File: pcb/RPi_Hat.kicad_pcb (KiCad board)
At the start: 2 copper layers, 65 x 56.5 mm, 31 parts, among them J1 RPi_GPIO, P1 Flow Meter, P2 Extra, P3 1 Wire, P4 Display, P5 Laser Controller, Q1 BSS138, Q2 PN2222A, Q3 BSS138, Q4 BSS138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

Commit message: Schematic updates
Don't use a relay, use a level shifter so the pin can be used as either
an input or an output.
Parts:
- removed D1: DIODE, Diodes_SMD:SMA_Handsoldering
- removed RL1: G5Q-14, Relays:Relay_SPDS_OMRON-G5Q
- added R3: 10k, Resistors_SMD:R_1206_HandSoldering, F.Cu at (102.9, 95.2)
- P2: footprint Terminal_Blocks:TerminalBlock_Pheonix_MPT-2.54mm_5pol -> Terminal_Blocks:TerminalBlock_Pheonix_MPT-2.54mm_4pol
- Q2: value PN2222A -> BSS138
- R4: value 1k -> 10k
- moved Q2 1.27 mm to (96.5, 95.2), turned to 90 degrees
- moved Q5 1.27 mm to (134.6, 82.5)
- moved R4 1.27 mm to (96.5, 91.4), turned to 180 degrees
- moved R7 1.27 mm to (130.8, 91.4)
- moved R9 1.27 mm to (130.8, 82.5)
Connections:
- net Net-(P1-Pad2) renamed FLOW_INPUT
- P2 pad 3: LP2 -> EP1
- P2 pad 4: EP1 -> +5V
- Q2 pad 1: GND -> +3V3
- Q2 pad 2: Net-(Q2-Pad2) -> LIGHTS
- Q2 pad 3: Net-(D1-Pad2) -> LP1
- R4 pad 1: Net-(Q2-Pad2) -> +5V
- R4 pad 2: LIGHTS -> LP1
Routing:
- net LP2: track 54.5 -> 0.00 mm
- net LP1: track 39.2 -> 8.57 mm
- net +3V3: track 130.4 -> 148.7 mm
- net +5V: track 142.7 -> 127.9 mm, vias 7 -> 5
- net LIGHTS: track 48.5 -> 58.8 mm
- net Net-(D1-Pad2): track 9.47 -> 0.00 mm
- net GND: track 223.0 -> 215.5 mm
- net Net-(Q2-Pad2): track 6.43 -> 0.00 mm
- net LC_AIR: track 55.4 -> 57.1 mm, vias 2 -> 0
- net LC4: track 27.0 -> 25.7 mm
- net EP1: track 13.6 -> 14.7 mm
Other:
- board text added: "Display"
- board text added: "Extra"
- board text added: "Laser"

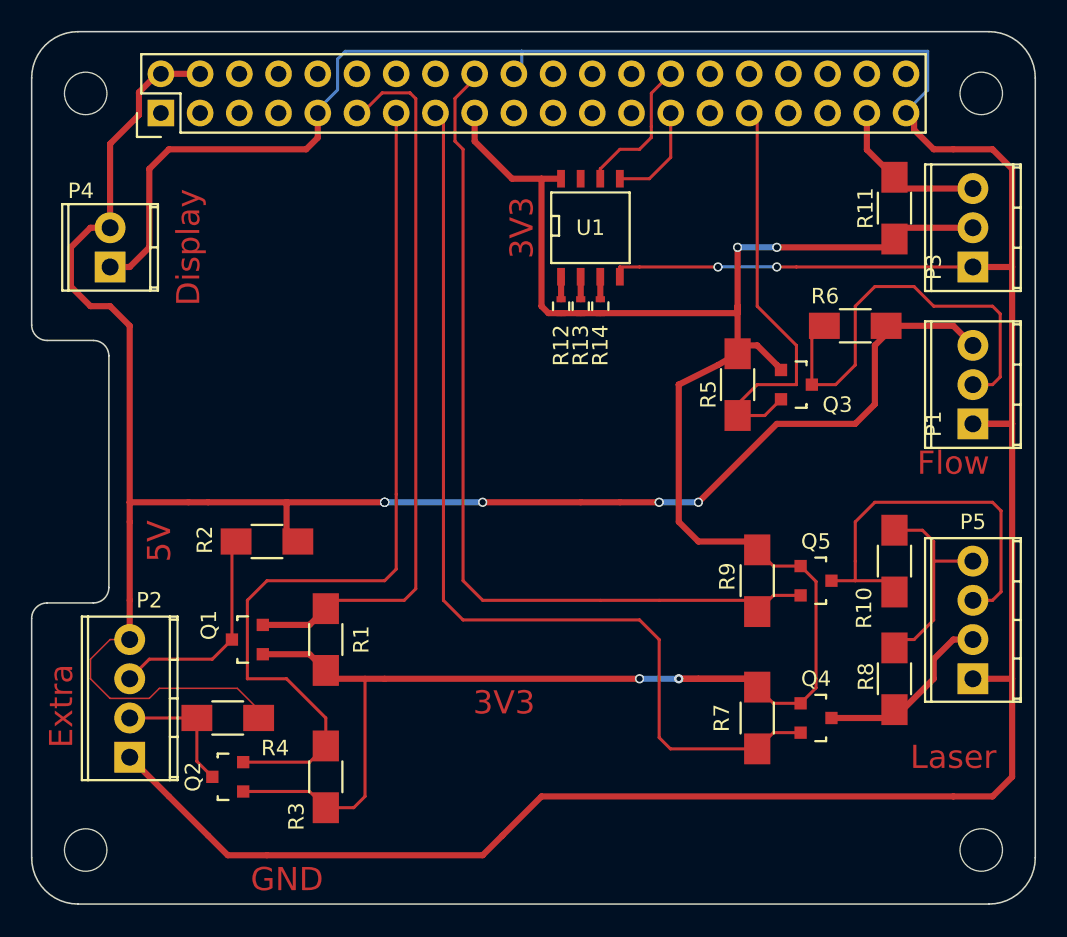
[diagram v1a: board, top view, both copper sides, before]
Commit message: Add outputs
for the chiller, exhaust, air
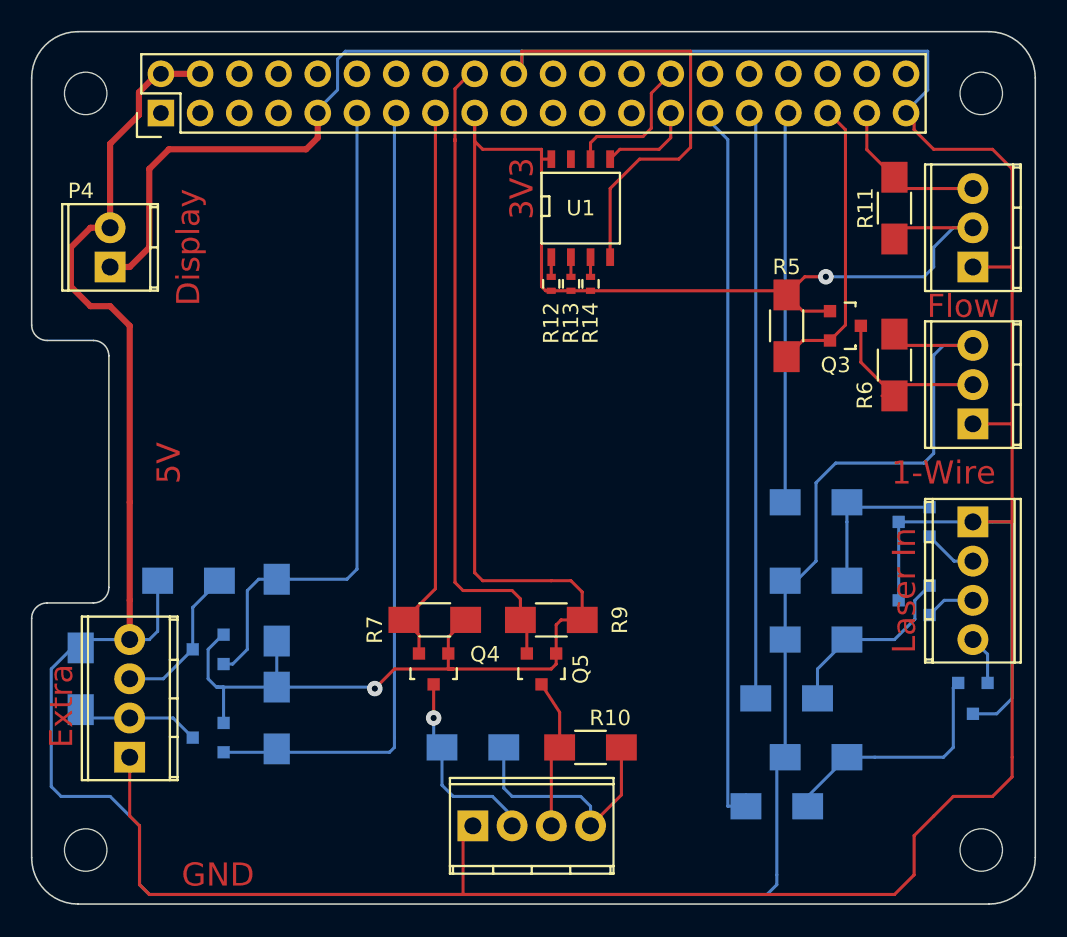
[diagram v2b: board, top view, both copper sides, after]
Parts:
- added P6: Laser Controller, Terminal_Blocks:TerminalBlock_Pheonix_MPT-2.54mm_4pol, F.Cu at (144.8, 78.7)
- added Q6: PZT2222A, TO_SOT_Packages_SMD:SOT-23, B.Cu at (144.8, 90.2)
- added Q7: PZT2222A, TO_SOT_Packages_SMD:SOT-23, B.Cu at (141.0, 83.8)
- added Q8: PZT2222A, TO_SOT_Packages_SMD:SOT-23, B.Cu at (141.0, 78.7)
- added R15: 4K7, Resistors_SMD:R_1206_HandSoldering, B.Cu at (132.1, 97.2)
- added R16: 4K7, Resistors_SMD:R_1206_HandSoldering, B.Cu at (132.7, 90.2)
- added R17: 4K7, Resistors_SMD:R_1206_HandSoldering, B.Cu at (134.6, 77.5)
- added R18: 4K7, Resistors_SMD:R_1206_HandSoldering, B.Cu at (134.6, 94.0)
- added R19: 4K7, Resistors_SMD:R_1206_HandSoldering, B.Cu at (134.6, 86.4)
- added R20: 4K7, Resistors_SMD:R_1206_HandSoldering, B.Cu at (134.6, 82.5)
- Q1, Q2, R1, R2, R3, R4, R8: moved to B.Cu
- moved P5 33.8 mm to (112.4, 98.4), turned to 0 degrees
- moved R8 27.7 mm to (112.4, 93.3), turned to 180 degrees
- moved Q4 25.0 mm to (109.9, 88.3), turned to 180 degrees
- moved R10 23.1 mm to (120.0, 93.3), turned to 0 degrees
- moved R7 21.8 mm to (109.9, 85.1), turned to 0 degrees
- moved Q5 18.7 mm to (116.8, 88.3), turned to 180 degrees
- moved R9 13.6 mm to (117.5, 85.1), turned to 0 degrees
- moved R4 9.86 mm to (87.0, 88.9), turned to 270 degrees
- moved R2 5.68 mm to (94.0, 82.5), turned to 0 degrees
- moved R3 4.96 mm to (99.7, 91.4), turned to 90 degrees
- moved Q3 4.96 mm to (136.5, 66.0)
- moved R5 4.96 mm to (132.7, 66.0)
- moved R1 3.70 mm to (99.7, 84.5)
- moved R6 3.59 mm to (139.7, 68.6), turned to 270 degrees
- moved Q2 2.84 mm to (95.2, 92.7), turned to 270 degrees
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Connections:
- J1 pad 29: (no net) -> OUT_EXHAUST
- J1 pad 31: FLOW_METER -> OUT_CHILLER
- J1 pad 33: (no net) -> OUT_AIR
- J1 pad 35: (no net) -> FLOW_METER
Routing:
- net OUT_EXHAUST: track 0.00 -> 47.3 mm
- net GND: track 215.5 -> 258.9 mm, vias 2 -> 0
- net +5V: track 127.9 -> 170.2 mm, vias 5 -> 0
- net OUT_CHILLER: track 0.00 -> 38.1 mm
- net LC_WORKING: track 63.6 -> 36.3 mm
- net OUT_AIR: track 0.00 -> 25.3 mm
- net Net-(Q6-Pad1): track 0.00 -> 16.1 mm
- net FLOW_INPUT: track 28.0 -> 12.3 mm
- net LC4: track 25.7 -> 11.0 mm
- net LC_AIR: track 57.1 -> 43.3 mm
- net Net-(Q7-Pad1): track 0.00 -> 12.2 mm
- net +3V3: track 148.7 -> 137.3 mm, vias 4 -> 2
- net Net-(Q8-Pad1): track 0.00 -> 10.6 mm
- net FLOW_METER: track 27.0 -> 18.9 mm
- net LIGHTS: track 58.8 -> 52.3 mm
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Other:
- net class Default: via_dia 0.6 -> 1
- board text added: "1-Wire"
- board text added: "Laser In"
- board text removed: "Laser"

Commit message: Add passives for the EEPROM
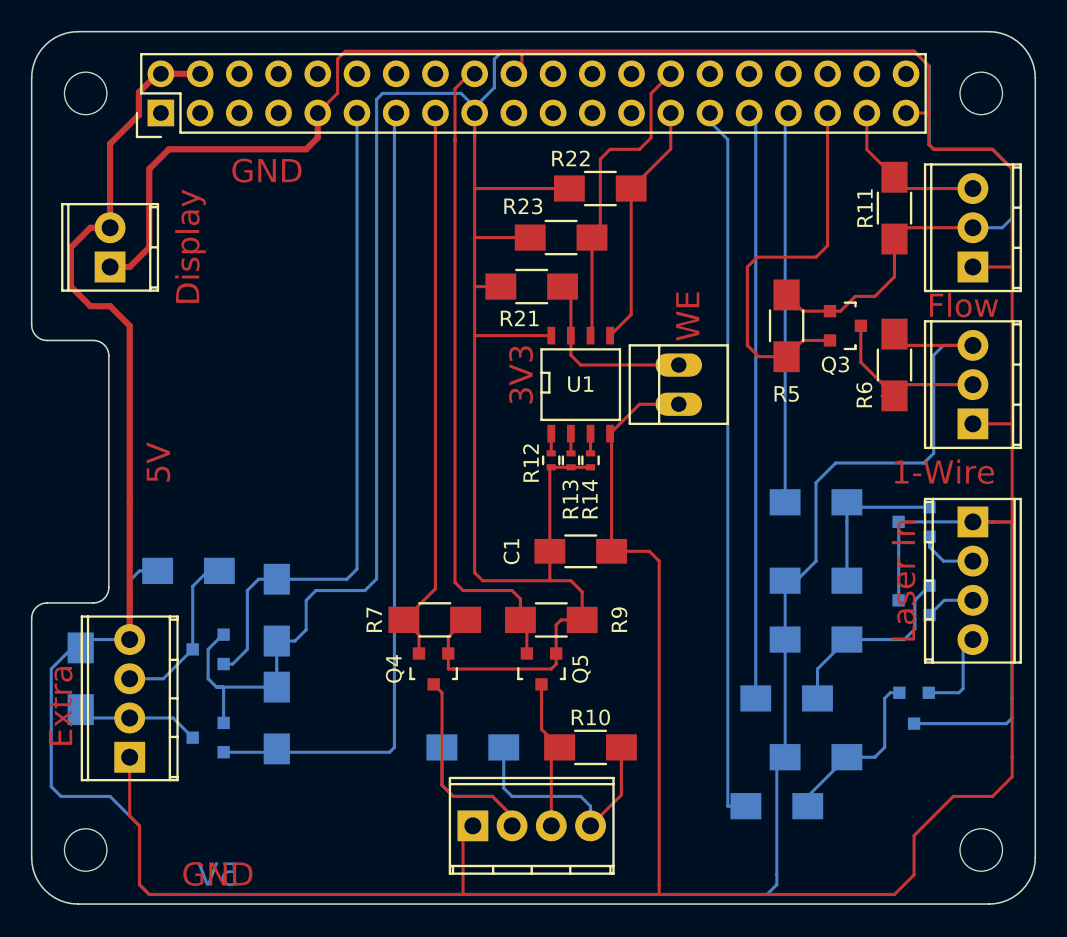
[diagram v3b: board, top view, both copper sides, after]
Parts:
- added C1: 100NF, Capacitors_SMD:C_1206_HandSoldering, F.Cu at (119.4, 80.6)
- added JP1: Jumper_NO_Small, Connect:PINHEAD1-2, F.Cu at (125.7, 69.8)
- added R21: 1K, Resistors_SMD:R_1206_HandSoldering, F.Cu at (116.2, 63.5)
- added R22: 3.9K, Resistors_SMD:R_1206_HandSoldering, F.Cu at (120.7, 57.1)
- added R23: 3.9K, Resistors_SMD:R_1206_HandSoldering, F.Cu at (118.1, 60.3)
- moved R12 11.4 mm to (117.5, 74.8)
- moved R13 11.4 mm to (118.8, 74.8)
- moved R14 11.4 mm to (120.0, 74.8)
- moved U1 11.4 mm to (119.4, 69.8)
- moved Q6 3.86 mm to (141.0, 90.8)
- moved R2 0.63 mm to (94.0, 81.9)
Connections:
- U1 pad 7: (no net) -> Net-(JP1-Pad2)
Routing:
- net +3V3: track 137.3 -> 213.5 mm, vias 2 -> 0
- net GND: track 258.9 -> 271.4 mm
- net Net-(JP1-Pad2): track 0.00 -> 11.9 mm
- net ID_SC: track 9.43 -> 20.2 mm
- net ID_SD: track 6.10 -> 16.0 mm
- net LC2: track 12.8 -> 22.0 mm, vias 1 -> 0
- net FLOW_METER: track 18.9 -> 25.7 mm
- net Net-(Q6-Pad1): track 16.1 -> 11.2 mm
- net HEADER_EXHAUST: track 3.20 -> 5.77 mm
- net EP1: track 10.0 -> 11.1 mm
- net +5V: track 170.2 -> 170.8 mm
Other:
- board text added: "WE"

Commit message: Add labels to pcb
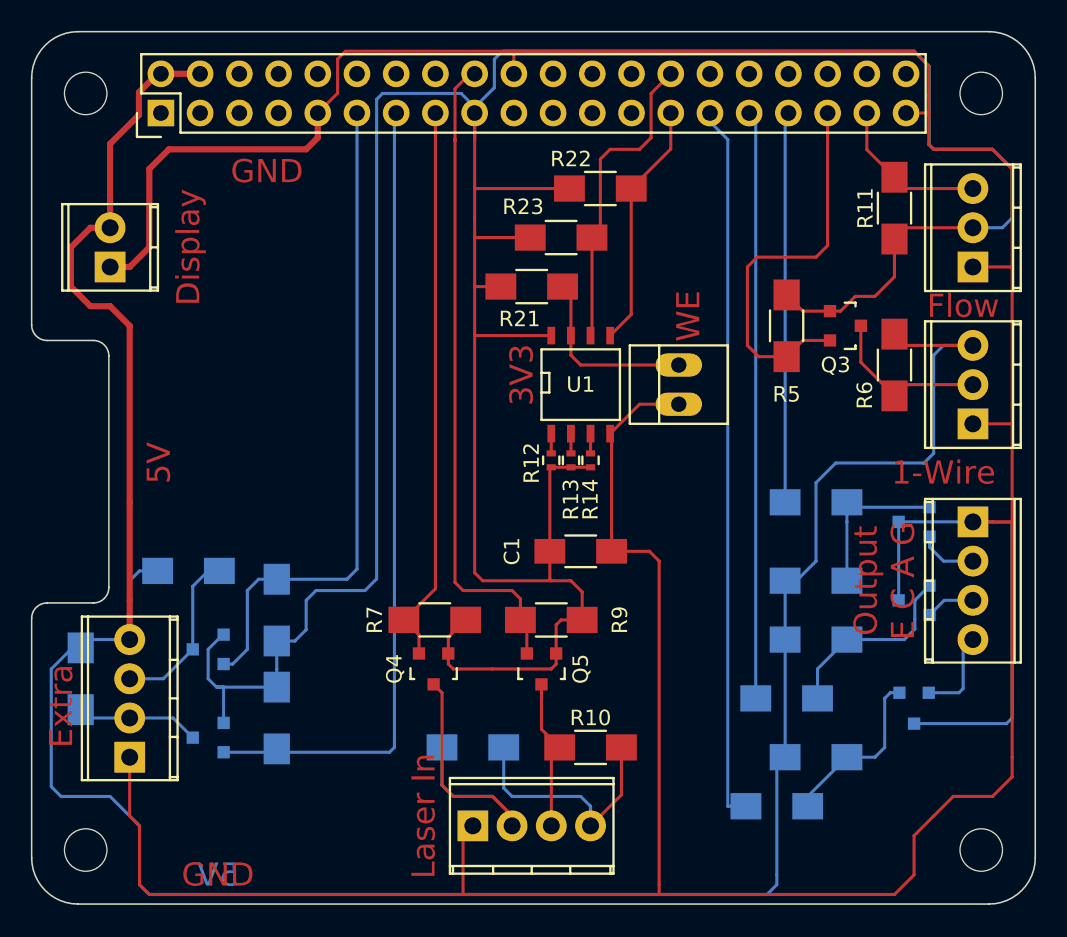
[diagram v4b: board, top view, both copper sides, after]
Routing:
- net GND: track 271.4 -> 270.6 mm
- net FLOW_INPUT: track 12.3 -> 11.5 mm
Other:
- net class Default: via_dia 1 -> 1.6; via_drill 0.4 -> 1.5
- board text added: "Output E C A G"

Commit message: Update the schematic
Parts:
- removed Q3: BSS138, TO_SOT_Packages_SMD:SOT-23
- removed R5, R6: 10k, Resistors_SMD:R_1206_HandSoldering
- added JP2: Relay Voltage Selector, Connect:PINHEAD1-3, F.Cu at (132.1, 100.3)
- P5: value Laser Controller -> Laser Controller Input
- P6: value Laser Controller -> Chiller/Air/Exhaust
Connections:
- P1 pad 2: FLOW_INPUT -> FLOW_METER
- P1 pad 3: +5V -> +3V3
- R18 pad 1: +5V -> VSS
- R19 pad 1: +5V -> VSS
- R20 pad 1: +5V -> VSS
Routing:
- net +5V: track 170.8 -> 124.0 mm
- net VSS: track 0.00 -> 20.3 mm
- net FLOW_INPUT: track 11.5 -> 0.00 mm
- net +3V3: track 213.3 -> 212.6 mm
